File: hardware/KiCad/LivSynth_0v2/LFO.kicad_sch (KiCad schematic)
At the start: 19 parts, among them Q1 2N3904, Q15 2N3904, Q16 2N3904, U3 TL074, U8 TL074

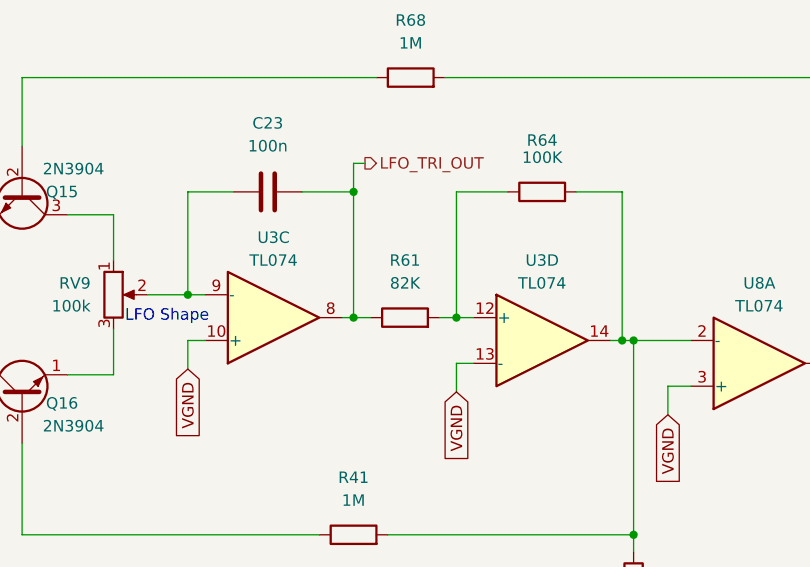
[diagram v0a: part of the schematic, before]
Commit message: Analog redesign:  - Power: Add voltage and current test points  - MCU: use PA11/PA12 for USB DFU interface  - MCU: add NRST reset switch  - Slew: increase portamento cap  - VCO: invert trim pots  - VCF: let resonance kick in earlier  - VCF: invert pots  - VCA: invert trim pot  - EG: full redesign, properly referencing VGND now  - LFO: R61 = 51K  - ModMatrix: add EG attenuverters  - IO: invert pots  - IO: limit output gain for 1W speaker  - IO: connect BTN_SHIFT in gap free order to SR
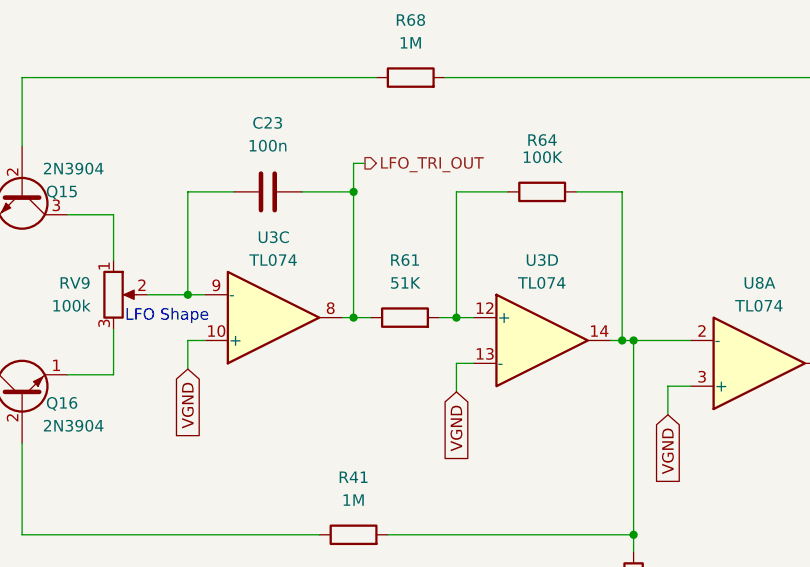
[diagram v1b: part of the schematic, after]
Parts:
- R61: value 82K -> 51K
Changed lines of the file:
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@@
     (in_bom yes) (on_board yes) (fields_autoplaced)
     (property "Reference" "R61" (id 0) (at 139.7 69.85 90))
-    (property "Value" "82K" (id 1) (at 139.7 72.39 90))
+    (property "Value" "51K" (id 1) (at 139.7 72.39 90))
     (property "Footprint" "Resistor_THT:R_Axial_DIN0207_L6.3mm_D2.5mm_P7.62mm_Horizontal" (id 2) (at 139.7 77.978 90)
       (effects (font (size 1.27 1.27)) hide)

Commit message: Analog Redesign:  - Power: Build ververse polarity protection using P-Mosfet and Zener Diode      - (https://www.youtube.com/watch?v=Ltx4vovY5Z4 - 1:28)  - Power: Build adjustable buck regulator for 8-9V stable voltage source  - PCB: Add location for order number ("JLCJLCJLCJLC")  - General: Add Tooling Holes for PCB assembly  - PCB: check frontend component layout for symmetry  - VCF: fix sound issues  - PCB: Add SloBlo icon  - PCB: Add switch labels to front side  - EG: test new design  - MCU: Add some debug pins
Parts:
- U3, U8: LCSC (none) -> C2057504
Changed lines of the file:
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@@
+      (effects (font (size 1.27 1.27)) hide)
+    )
+    (property "LCSC" "C2057504" (id 4) (at 154.94 78.74 0)
       (effects (font (size 1.27 1.27)) hide)
     )
@@
       (effects (font (size 1.27 1.27)) hide)
     )
+    (property "LCSC" "C2057504" (id 4) (at 125.095 76.2 0)
+      (effects (font (size 1.27 1.27)) hide)
+    )
     (pin "1")
     (pin "2")
@@
       (effects (font (size 1.27 1.27)) hide)
     )
+    (property "LCSC" "C2057504" (id 4) (at 179.07 81.28 0)
+      (effects (font (size 1.27 1.27)) hide)
+    )

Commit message: progress 2023-01-21
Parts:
- C23: value 100n -> 1u; footprint Capacitor_THT:C_Rect_L7.2mm_W2.5mm_P5.00mm_FKS2_FKP2_MKS2_MKP2 -> Capacitor_THT:C_Rect_L7.2mm_W5.5mm_P5.00mm_FKS2_FKP2_MKS2_MKP2
- renumbered U3 to U8
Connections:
- net LFO_TRI_OUT: now also U8.7; no longer U8.8
- net VGND: now also U8.5 (+); no longer U8.10 (+)
- net at C23.1, RV9.2: now also U8.6 (-); no longer U8.9 (-)
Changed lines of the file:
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@@
   (symbol (lib_id "Amplifier_Operational:TL074") (at 154.94 78.74 0) (unit 4)
     (in_bom yes) (on_board yes)
-    (property "Reference" "U3" (id 0) (at 154.94 69.85 0))
+    (property "Reference" "U8" (id 0) (at 154.94 69.85 0))
     (property "Value" "TL074" (id 1) (at 154.94 72.39 0))
     (property "Footprint" "Package_SO:SOIC-14_3.9x8.7mm_P1.27mm" (id 2) (at 153.67 76.2 0)
@@
     (in_bom yes) (on_board yes) (fields_autoplaced)
     (property "Reference" "C23" (id 0) (at 124.46 54.61 90))
-    (property "Value" "100n" (id 1) (at 124.46 57.15 90))
-    (property "Footprint" "Capacitor_THT:C_Rect_L7.2mm_W2.5mm_P5.00mm_FKS2_FKP2_MKS2_MKP2" (id 2) (at 128.27 61.2648 0)
+    (property "Value" "1u" (id 1) (at 124.46 57.15 90))
+    (property "Footprint" "Capacitor_THT:C_Rect_L7.2mm_W5.5mm_P5.00mm_FKS2_FKP2_MKS2_MKP2" (id 2) (at 128.27 61.2648 0)
       (effects (font (size 1.27 1.27)) hide)
     )
@@
     (pin "2")
   )
-  (symbol (lib_id "Amplifier_Operational:TL074") (at 125.095 76.2 0) (mirror x) (unit 3)
+  (symbol (lib_id "Amplifier_Operational:TL074") (at 125.095 76.2 0) (mirror x) (unit 2)
     (in_bom yes) (on_board yes)
-    (property "Reference" "U3" (id 0) (at 125.095 67.31 0))
+    (property "Reference" "U8" (id 0) (at 125.095 67.31 0))
     (property "Value" "TL074" (id 1) (at 125.095 69.85 0))
     (property "Footprint" "Package_SO:SOIC-14_3.9x8.7mm_P1.27mm" (id 2) (at 123.825 78.74 0)

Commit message: Geographical reannotate
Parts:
- renumbered C23 to C25, D2 to D1, D6 to D8, Q15 to Q17, R4 to R3, R19 to R42, R22 to R50, R40 to R54, R41 to R62, R68 to R63, R61 to R71, R64 to R72, RV9 to RV11, RV5 to RV7, U8 to U6
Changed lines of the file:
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@@
   (symbol (lib_id "Amplifier_Operational:TL074") (at 154.94 78.74 0) (unit 4)
     (in_bom yes) (on_board yes)
-    (property "Reference" "U8" (id 0) (at 154.94 69.85 0))
+    (property "Reference" "U6" (id 0) (at 154.94 69.85 0))
     (property "Value" "TL074" (id 1) (at 154.94 72.39 0))
     (property "Footprint" "Package_SO:SOIC-14_3.9x8.7mm_P1.27mm" (id 2) (at 153.67 76.2 0)
@@
   (symbol (lib_id "Device:R") (at 139.7 76.2 90) (unit 1)
     (in_bom yes) (on_board yes) (fields_autoplaced)
-    (property "Reference" "R61" (id 0) (at 139.7 69.85 90))
+    (property "Reference" "R71" (id 0) (at 139.7 69.85 90))
     (property "Value" "51K" (id 1) (at 139.7 72.39 90))
     (property "Footprint" "Resistor_THT:R_Axial_DIN0207_L6.3mm_D2.5mm_P7.62mm_Horizontal" (id 2) (at 139.7 77.978 90)
@@
   (symbol (lib_id "Device:R") (at 165.1 129.54 0) (unit 1)
     (in_bom yes) (on_board yes) (fields_autoplaced)
-    (property "Reference" "R40" (id 0) (at 167.64 128.2699 0)
+    (property "Reference" "R54" (id 0) (at 167.64 128.2699 0)
       (effects (font (size 1.27 1.27)) (justify left))
     )
@@
   (symbol (lib_id "Device:C") (at 124.46 62.23 90) (unit 1)
     (in_bom yes) (on_board yes) (fields_autoplaced)
-    (property "Reference" "C23" (id 0) (at 124.46 54.61 90))
+    (property "Reference" "C25" (id 0) (at 124.46 54.61 90))
     (property "Value" "1u" (id 1) (at 124.46 57.15 90))
     (property "Footprint" "Capacitor_THT:C_Rect_L7.2mm_W5.5mm_P5.00mm_FKS2_FKP2_MKS2_MKP2" (id 2) (at 128.27 61.2648 0)
@@
   (symbol (lib_id "Device:R") (at 201.93 62.23 270) (unit 1)
     (in_bom yes) (on_board yes) (fields_autoplaced)
-    (property "Reference" "R4" (id 0) (at 201.93 56.515 90))
+    (property "Reference" "R3" (id 0) (at 201.93 56.515 90))
     (property "Value" "100K" (id 1) (at 201.93 59.055 90))
     (property "Footprint" "Resistor_THT:R_Axial_DIN0207_L6.3mm_D2.5mm_P7.62mm_Horizontal" (id 2) (at 201.93 60.452 90)
@@
   (symbol (lib_id "Device:R_Potentiometer") (at 107.315 73.66 0) (unit 1)
     (in_bom yes) (on_board yes) (fields_autoplaced)
-    (property "Reference" "RV9" (id 0) (at 104.775 72.3899 0)
+    (property "Reference" "RV11" (id 0) (at 104.775 72.3899 0)
       (effects (font (size 1.27 1.27)) (justify right))
     )
@@
   (symbol (lib_id "Device:R") (at 133.985 117.475 270) (unit 1)
     (in_bom yes) (on_board yes) (fields_autoplaced)
-    (property "Reference" "R22" (id 0) (at 133.985 111.76 90))
+    (property "Reference" "R50" (id 0) (at 133.985 111.76 90))
     (property "Value" "100R" (id 1) (at 133.985 114.3 90))
     (property "Footprint" "Resistor_THT:R_Axial_DIN0207_L6.3mm_D2.5mm_P7.62mm_Horizontal" (id 2) (at 133.985 115.697 90)
@@
   (symbol (lib_id "Device:R_Potentiometer") (at 165.1 117.475 180) (unit 1)
     (in_bom yes) (on_board yes) (fields_autoplaced)
-    (property "Reference" "RV5" (id 0) (at 167.64 116.2049 0)
+    (property "Reference" "RV7" (id 0) (at 167.64 116.2049 0)
       (effects (font (size 1.27 1.27)) (justify right))
     )
@@
   (symbol (lib_id "Device:R") (at 140.335 49.53 90) (unit 1)
     (in_bom yes) (on_board yes) (fields_autoplaced)
-    (property "Reference" "R68" (id 0) (at 140.335 43.18 90))
+    (property "Reference" "R63" (id 0) (at 140.335 43.18 90))
     (property "Value" "1M" (id 1) (at 140.335 45.72 90))
     (property "Footprint" "Resistor_THT:R_Axial_DIN0207_L6.3mm_D2.5mm_P7.62mm_Horizontal" (id 2) (at 140.335 51.308 90)
@@
   (symbol (lib_id "Amplifier_Operational:TL074") (at 125.095 76.2 0) (mirror x) (unit 2)
     (in_bom yes) (on_board yes)
-    (property "Reference" "U8" (id 0) (at 125.095 67.31 0))
+    (property "Reference" "U6" (id 0) (at 125.095 67.31 0))
     (property "Value" "TL074" (id 1) (at 125.095 69.85 0))
     (property "Footprint" "Package_SO:SOIC-14_3.9x8.7mm_P1.27mm" (id 2) (at 123.825 78.74 0)
@@
   (symbol (lib_id "Transistor_BJT:2N3904") (at 97.155 62.23 270) (unit 1)
     (in_bom yes) (on_board yes)
-    (property "Reference" "Q15" (id 0) (at 101.6 62.23 90))
+    (property "Reference" "Q17" (id 0) (at 101.6 62.23 90))
     (property "Value" "2N3904" (id 1) (at 102.87 59.69 90))
     (property "Footprint" "Package_TO_SOT_THT:TO-92_Inline" (id 2) (at 95.25 67.31 0)
@@
   (symbol (lib_id "Amplifier_Operational:TL074") (at 179.07 81.28 0) (mirror x) (unit 1)
     (in_bom yes) (on_board yes)
-    (property "Reference" "U8" (id 0) (at 179.07 72.39 0))
+    (property "Reference" "U6" (id 0) (at 179.07 72.39 0))
     (property "Value" "TL074" (id 1) (at 179.07 74.93 0))
     (property "Footprint" "Package_SO:SOIC-14_3.9x8.7mm_P1.27mm" (id 2) (at 177.8 83.82 0)
@@
   (symbol (lib_id "Device:LED") (at 217.17 83.82 90) (unit 1)
     (in_bom yes) (on_board yes) (fields_autoplaced)
-    (property "Reference" "D6" (id 0) (at 220.98 84.1374 90)
+    (property "Reference" "D8" (id 0) (at 220.98 84.1374 90)
       (effects (font (size 1.27 1.27)) (justify right))
     )
@@
   (symbol (lib_id "Device:R") (at 133.985 100.33 90) (unit 1)
     (in_bom yes) (on_board yes) (fields_autoplaced)
-    (property "Reference" "R41" (id 0) (at 133.985 93.98 90))
+    (property "Reference" "R62" (id 0) (at 133.985 93.98 90))
     (property "Value" "1M" (id 1) (at 133.985 96.52 90))
     (property "Footprint" "Resistor_THT:R_Axial_DIN0207_L6.3mm_D2.5mm_P7.62mm_Horizontal" (id 2) (at 133.985 102.108 90)
@@
   (symbol (lib_id "Device:R") (at 154.94 62.23 90) (unit 1)
     (in_bom yes) (on_board yes)
-    (property "Reference" "R64" (id 0) (at 154.94 56.515 90))
+    (property "Reference" "R72" (id 0) (at 154.94 56.515 90))
     (property "Value" "100K" (id 1) (at 154.94 58.42 90))
     (property "Footprint" "Resistor_THT:R_Axial_DIN0207_L6.3mm_D2.5mm_P7.62mm_Horizontal" (id 2) (at 154.94 64.008 90)
@@
   (symbol (lib_id "Device:LED") (at 217.17 73.66 90) (unit 1)
     (in_bom yes) (on_board yes) (fields_autoplaced)
-    (property "Reference" "D2" (id 0) (at 220.98 73.9774 90)
+    (property "Reference" "D1" (id 0) (at 220.98 73.9774 90)
       (effects (font (size 1.27 1.27)) (justify right))
     )
@@
   (symbol (lib_id "Device:R") (at 165.1 106.045 0) (unit 1)
     (in_bom yes) (on_board yes) (fields_autoplaced)
-    (property "Reference" "R19" (id 0) (at 167.64 104.7749 0)
-      (effects (font (size 1.27 1.27)) (justify left))
-    )
+    (property "Reference" "R42" (id 0) (at 167.64 104.7749 0)
+      (effects (font (size 1.27 1.27)) (justify left))
+    )

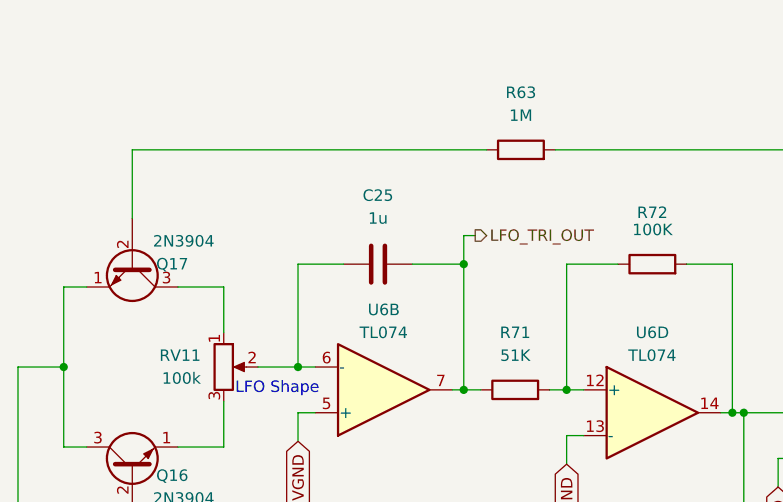
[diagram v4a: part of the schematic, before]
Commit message: Reduce EG cap to 4u7 Reduce LFO cap to 220n VCO R23: 470K, C13: 10n
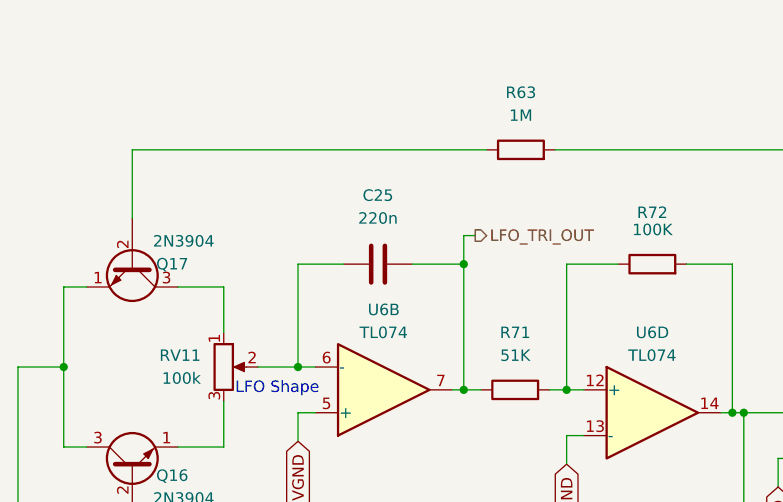
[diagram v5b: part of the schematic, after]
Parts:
- C25: value 1u -> 220n

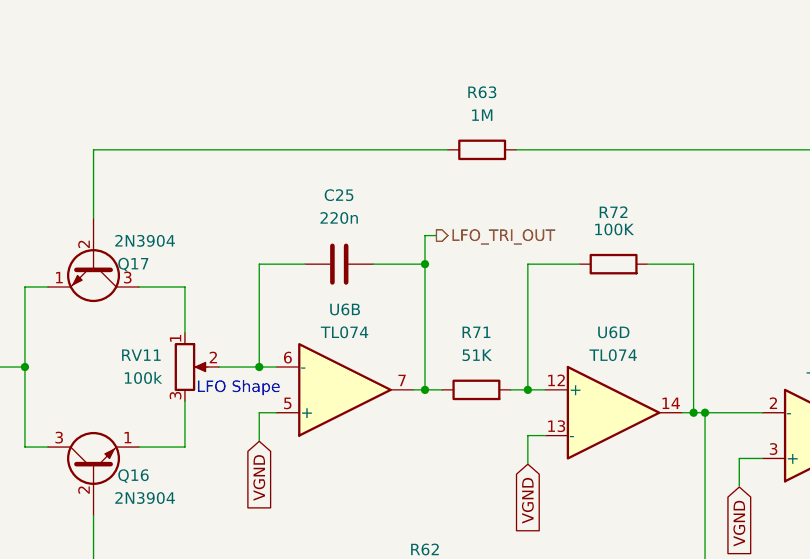
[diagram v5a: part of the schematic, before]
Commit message: EG: raise Rf of comparator circuit to improve performance LFO: raise coupling resistor for higher amplitude, adapt cap for more musical ranges
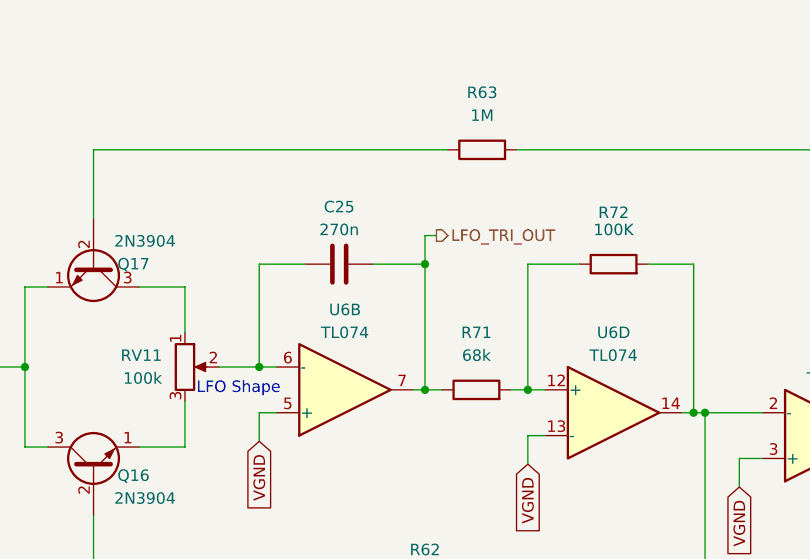
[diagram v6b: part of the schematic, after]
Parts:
- C25: value 220n -> 270n
- R71: value 51K -> 68k
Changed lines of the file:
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@@
       (effects (font (size 1.27 1.27)))
     )
-    (property "Value" "51K" (at 139.7 72.39 90)
+    (property "Value" "68k" (at 139.7 72.39 90)
       (effects (font (size 1.27 1.27)))
     )
@@
   (symbol (lib_id "Device:C") (at 124.46 62.23 90) (unit 1)
     (in_bom yes) (on_board yes) (dnp no) (fields_autoplaced)
-    (property "Reference" "C25" (at 124.46 54.61 90)
+    (property "Reference" "C25" (at 124.46 55.88 90)
       (effects (font (size 1.27 1.27)))
     )
-    (property "Value" "220n" (at 124.46 57.15 90)
+    (property "Value" "270n" (at 124.46 58.42 90)
       (effects (font (size 1.27 1.27)))
     )
